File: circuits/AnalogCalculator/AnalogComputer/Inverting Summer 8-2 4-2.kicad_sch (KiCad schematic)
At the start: 9 parts, among them U11 LM324

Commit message: update layount
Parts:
- R53, R54, R55, R56: footprint Resistor_THT_US_AKL:R_Box_L8.4mm_W2.5mm_P5.08mm -> Resistor_THT:R_Axial_DIN0204_L3.6mm_D1.6mm_P2.54mm_Vertical
- RN5, RN7: footprint Resistor_THT_US_AKL:R_Array_SIP5_BigPads -> Resistor_THT:R_Array_SIP5
- RN6, RN8: footprint Resistor_THT_US_AKL:R_Array_SIP9_BigPads -> Resistor_THT:R_Array_SIP9
- U11: footprint (none) -> Package_DIP:DIP-14_W7.62mm_Socket
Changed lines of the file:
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@@
       (effects (font (size 1.27 1.27)))
     )
-    (property "Footprint" "" (at 85.09 38.1 0)
+    (property "Footprint" "Package_DIP:DIP-14_W7.62mm_Socket" (at 85.09 38.1 0)
       (effects (font (size 1.27 1.27)) hide)
     )
@@
       (effects (font (size 1.27 1.27)))
     )
-    (property "Footprint" "Resistor_THT_US_AKL:R_Box_L8.4mm_W2.5mm_P5.08mm" (at 96.52 97.79 0)
+    (property "Footprint" "Resistor_THT:R_Axial_DIN0204_L3.6mm_D1.6mm_P2.54mm_Vertical" (at 96.52 97.79 0)
       (effects (font (size 1.27 1.27)) hide)
     )
@@
       (effects (font (size 1.27 1.27)))
     )
-    (property "Footprint" "Resistor_THT_US_AKL:R_Array_SIP9_BigPads" (at 54.61 128.27 0)
+    (property "Footprint" "Resistor_THT:R_Array_SIP9" (at 54.61 128.27 0)
       (effects (font (size 1.27 1.27)) hide)
     )
@@
       (effects (font (size 1.27 1.27)))
     )
-    (property "Footprint" "Resistor_THT_US_AKL:R_Box_L8.4mm_W2.5mm_P5.08mm" (at 96.52 127 0)
+    (property "Footprint" "Resistor_THT:R_Axial_DIN0204_L3.6mm_D1.6mm_P2.54mm_Vertical" (at 96.52 127 0)
       (effects (font (size 1.27 1.27)) hide)
     )
@@
       (effects (font (size 1.27 1.27)))
     )
-    (property "Footprint" "" (at 85.09 113.03 0)
+    (property "Footprint" "Package_DIP:DIP-14_W7.62mm_Socket" (at 85.09 113.03 0)
       (effects (font (size 1.27 1.27)) hide)
     )
@@
       (effects (font (size 1.27 1.27)))
     )
-    (property "Footprint" "Resistor_THT_US_AKL:R_Box_L8.4mm_W2.5mm_P5.08mm" (at 96.52 74.93 0)
+    (property "Footprint" "Resistor_THT:R_Axial_DIN0204_L3.6mm_D1.6mm_P2.54mm_Vertical" (at 96.52 74.93 0)
       (effects (font (size 1.27 1.27)) hide)
     )
@@
       (effects (font (size 1.27 1.27)) (justify left))
     )
-    (property "Footprint" "" (at 254 39.37 0)
+    (property "Footprint" "Package_DIP:DIP-14_W7.62mm_Socket" (at 254 39.37 0)
       (effects (font (size 1.27 1.27)) hide)
     )
@@
       (effects (font (size 1.27 1.27)))
     )
-    (property "Footprint" "Resistor_THT_US_AKL:R_Array_SIP9_BigPads" (at 54.61 99.06 0)
+    (property "Footprint" "Resistor_THT:R_Array_SIP9" (at 54.61 99.06 0)
       (effects (font (size 1.27 1.27)) hide)
     )
@@
       (effects (font (size 1.27 1.27)))
     )
-    (property "Footprint" "" (at 85.09 60.96 0)
+    (property "Footprint" "Package_DIP:DIP-14_W7.62mm_Socket" (at 85.09 60.96 0)
       (effects (font (size 1.27 1.27)) hide)
     )
@@
       (effects (font (size 1.27 1.27)))
     )
-    (property "Footprint" "Resistor_THT_US_AKL:R_Array_SIP5_BigPads" (at 54.61 71.12 0)
+    (property "Footprint" "Resistor_THT:R_Array_SIP5" (at 54.61 71.12 0)
       (effects (font (size 1.27 1.27)) hide)
     )
@@
       (effects (font (size 1.27 1.27)))
     )
-    (property "Footprint" "Resistor_THT_US_AKL:R_Box_L8.4mm_W2.5mm_P5.08mm" (at 96.52 52.07 0)
+    (property "Footprint" "Resistor_THT:R_Axial_DIN0204_L3.6mm_D1.6mm_P2.54mm_Vertical" (at 96.52 52.07 0)
       (effects (font (size 1.27 1.27)) hide)
     )
@@
       (effects (font (size 1.27 1.27)))
     )
-    (property "Footprint" "Resistor_THT_US_AKL:R_Array_SIP5_BigPads" (at 54.61 48.26 0)
+    (property "Footprint" "Resistor_THT:R_Array_SIP5" (at 54.61 48.26 0)
       (effects (font (size 1.27 1.27)) hide)
     )
@@
       (effects (font (size 1.27 1.27)))
     )
-    (property "Footprint" "" (at 85.09 83.82 0)
-      (effects (font (size 1.27 1.27)) hide)
-    )
+    (property "Footprint" "Package_DIP:DIP-14_W7.62mm_Socket" (at 85.09 83.82 0)
+      (effects (font (size 1.27 1.27)) hide)
+    )

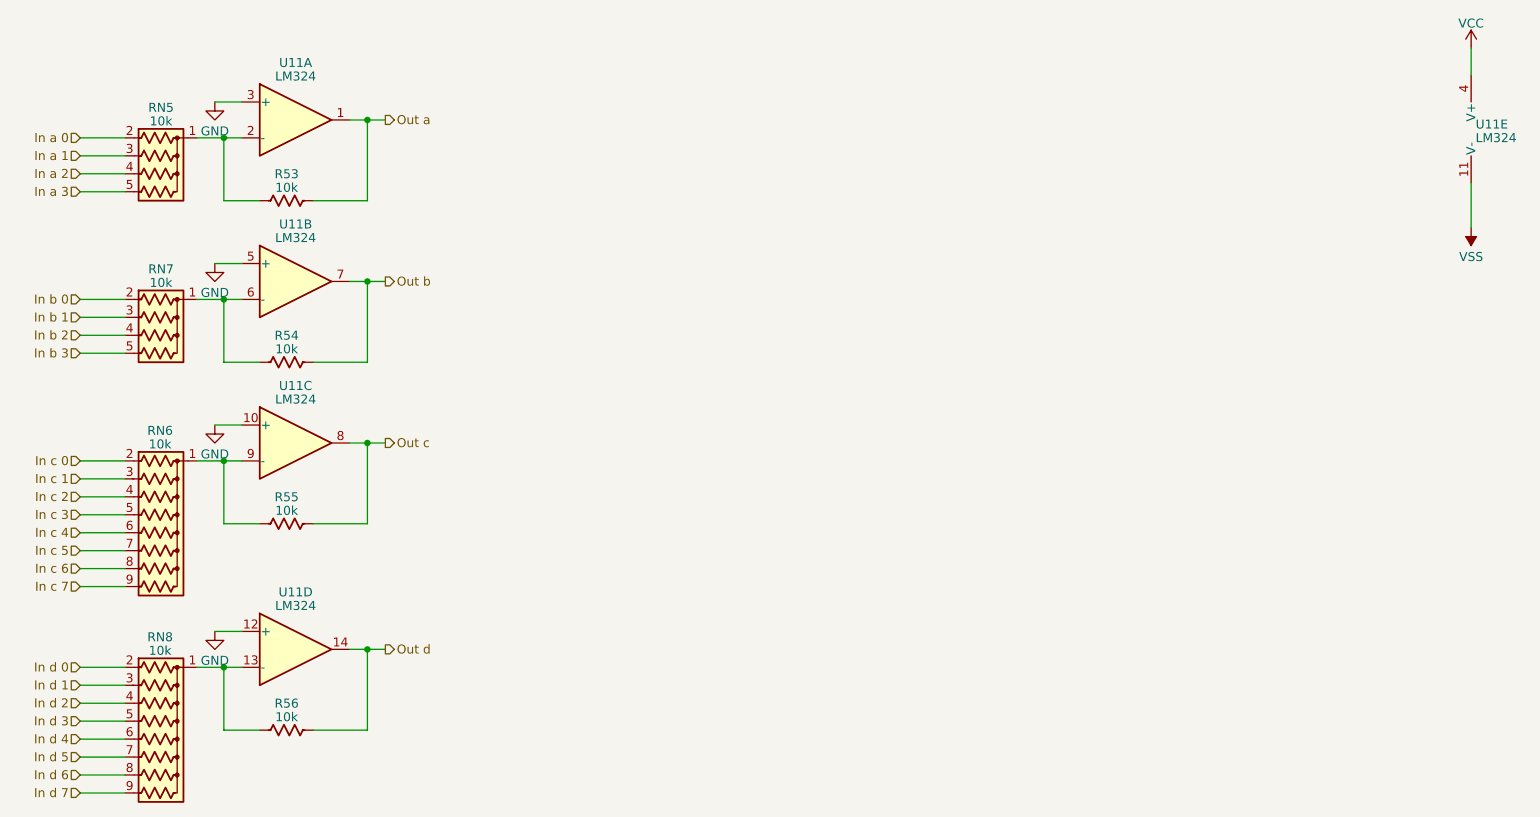
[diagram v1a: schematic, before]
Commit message: update analog computer layout
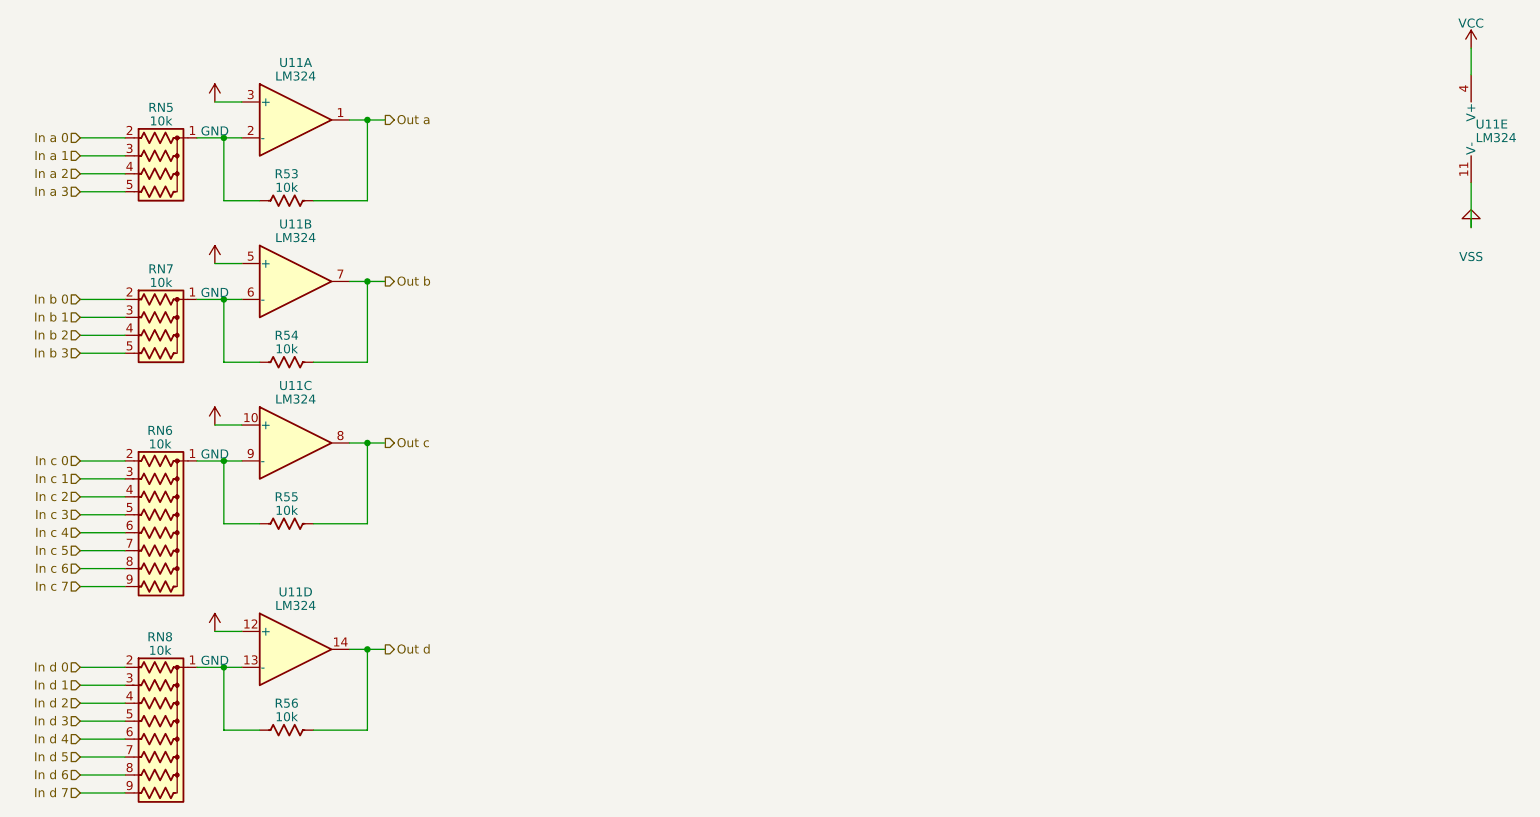
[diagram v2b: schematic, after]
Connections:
- net VSS is gone; now on net GND: U11.11 (V-)
- net GND: no longer U11.10 (+), U11.12 (+), U11.3 (+), U11.5 (+)
- new net VDD: U11.10 (+), U11.12 (+), U11.3 (+), U11.5 (+)
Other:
- company: (none) -> Out-of-band Development, LLC
- title: Inverting Summer 2x8 2x4 -> Analog Computer
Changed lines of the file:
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@@
   (paper "A4")
   (title_block
-    (title "Inverting Summer 2x8 2x4")
+    (title "Analog Computer")
+    (date "2023-03-08")
+    (rev "v1")
+    (company "Out-of-band Development, LLC")
+    (comment 1 "Matthew Whited")
+    (comment 2 "Inverting Summing Amplifier")
+    (comment 3 "2x8x10k with 10k Feedback")
+    (comment 4 "2x4x10k with 10k Feedback")
   )
   (junction (at 96.52 40.64) (diameter 0) (color 0 0 0 0)
@@
     )
   )
-  (symbol (lib_id "power:GND") (at 74.93 113.03 0) (unit 1)
+  (symbol (lib_id "power:VDD") (at 74.93 113.03 0) (unit 1)
     (in_bom yes) (on_board yes) (dnp no) (fields_autoplaced)
     (property "Reference" "#PWR040" (at 74.93 119.38 0)
@@
     )
   )
-  (symbol (lib_id "power:GND") (at 74.93 60.96 0) (unit 1)
+  (symbol (lib_id "power:VDD") (at 74.93 60.96 0) (unit 1)
     (in_bom yes) (on_board yes) (dnp no) (fields_autoplaced)
     (property "Reference" "#PWR038" (at 74.93 67.31 0)
@@
     )
   )
-  (symbol (lib_id "power:VSS") (at 252.73 55.88 180) (unit 1)
+  (symbol (lib_id "power:GND") (at 252.73 55.88 180) (unit 1)
     (in_bom yes) (on_board yes) (dnp no) (fields_autoplaced)
     (property "Reference" "#PWR042" (at 252.73 52.07 0)
@@
     )
   )
-  (symbol (lib_id "power:GND") (at 74.93 83.82 0) (unit 1)
+  (symbol (lib_id "power:VDD") (at 74.93 83.82 0) (unit 1)
     (in_bom yes) (on_board yes) (dnp no) (fields_autoplaced)
     (property "Reference" "#PWR039" (at 74.93 90.17 0)
@@
     )
   )
-  (symbol (lib_id "power:GND") (at 74.93 38.1 0) (unit 1)
+  (symbol (lib_id "power:VDD") (at 74.93 38.1 0) (unit 1)
     (in_bom yes) (on_board yes) (dnp no) (fields_autoplaced)
     (property "Reference" "#PWR037" (at 74.93 44.45 0)
